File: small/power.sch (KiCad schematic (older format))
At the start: 34 parts, among them J2 Screw_Terminal_01x02, Q4 AO3401A, U10 TPS5430DDAR, U2 LM7805_TO220, U20 TPS5430DDAR, U3 AMS1117-3.3

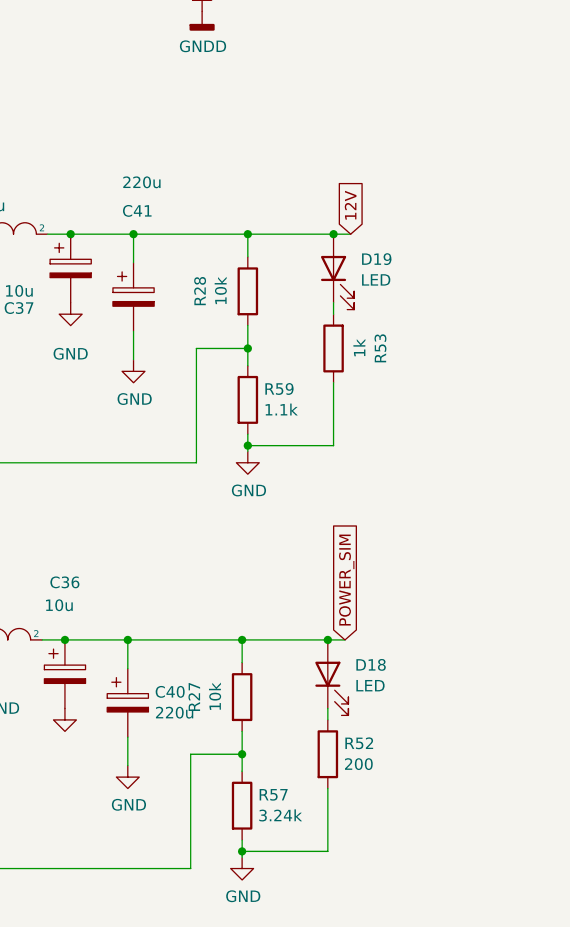
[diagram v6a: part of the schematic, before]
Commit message: ULN2003 footprint updated
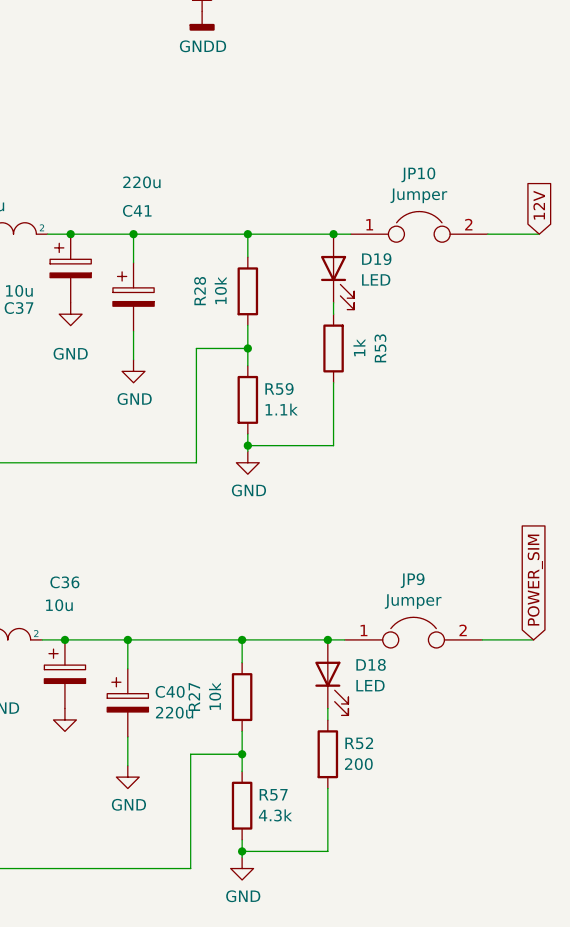
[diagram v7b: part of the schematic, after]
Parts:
- added JP10, JP9: Jumper, Jumper:SolderJumper-2_P1.3mm_Open_Pad1.0x1.5mm, symbol Device:Jumper
- R57: value 3.24k -> 4.3k; LCSC C22994 -> C23159; MPN 0603WAF3241T5E -> 0603WAF4301T5E
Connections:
- net 12V: now also JP10.2; no longer C37.1, C41.1, D19.2 (A), L2.2, R28.1
- net POWER_SIM: now also JP9.2; no longer C36.1, C40.1, D18.2 (A), L1.2, R27.1
- new net: C36.1, C40.1, D18.2 (A), JP9.1, L1.2, R27.1
- new net: C37.1, C41.1, D19.2 (A), JP10.1, L2.2, R28.1
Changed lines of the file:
@@
 P 7250 5075
 F 0 "R57" H 7320 5121 50  0000 L CNN
-F 1 "3.24k" H 7320 5030 50  0000 L CNN
+F 1 "4.3k" H 7320 5030 50  0000 L CNN
 F 2 "Resistor_SMD:R_0603_1608Metric" V 7180 5075 50  0001 C CNN
-F 3 "https://datasheet.lcsc.com/szlcsc/Uniroyal-Elec-0603WAF3241T5E_C22994.pdf" H 7250 5075 50  0001 C CNN
-F 4 "C22994" H 7250 5075 50  0001 C CNN "LCSC"
-F 5 "0603WAF3241T5E" H 7250 5075 50  0001 C CNN "MPN"
+F 3 "https://datasheet.lcsc.com/szlcsc/Uniroyal-Elec-0603WAF4301T5E_C23159.pdf" H 7250 5075 50  0001 C CNN
+F 4 "C23159" H 7250 5075 50  0001 C CNN "LCSC"
+F 5 "0603WAF4301T5E" H 7250 5075 50  0001 C CNN "MPN"
 F 6 "0.0016" H 7250 5075 50  0001 C CNN "Price"
 F 7 "0" H 7250 5075 50  0001 C CNN "source"
@@
 Wire Wire Line
 	7250 4850 7250 4925
-Text GLabel 7700 4350 1    50   Input ~ 0
+Text GLabel 8525 4350 1    50   Input ~ 0
 POWER_SIM
-Text GLabel 7725 2575 1    50   Input ~ 0
+Text GLabel 8550 2575 1    50   Input ~ 0
 12V
 Text GLabel 2825 2575 1    50   Input ~ 0
@@
 Wire Wire Line
 	7650 2575 7725 2575
+$Comp
+L Device:Jumper JP10
+U 1 1 603CB025
+P 8025 2575
+F 0 "JP10" H 8025 2839 50  0000 C CNN
+F 1 "Jumper" H 8025 2748 50  0000 C CNN
+F 2 "Jumper:SolderJumper-2_P1.3mm_Open_Pad1.0x1.5mm" H 8025 2575 50  0001 C CNN
+F 3 "~" H 8025 2575 50  0001 C CNN
+	1    8025 2575
+	1    0    0    -1
+$EndComp
+Wire Wire Line
+	8325 2575 8550 2575
+$Comp
+L Device:Jumper JP9
+U 1 1 603D3CFE
+P 8000 4350
+F 0 "JP9" H 8000 4614 50  0000 C CNN
+F 1 "Jumper" H 8000 4523 50  0000 C CNN
+F 2 "Jumper:SolderJumper-2_P1.3mm_Open_Pad1.0x1.5mm" H 8000 4350 50  0001 C CNN
+F 3 "~" H 8000 4350 50  0001 C CNN
+	1    8000 4350
+	1    0    0    -1
+$EndComp
+Wire Wire Line
+	8300 4350 8525 4350
 $EndSCHEMATC
